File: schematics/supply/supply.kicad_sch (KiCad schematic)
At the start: 9 parts, among them J1 Conn_01x02_Pin, J2 Conn_01x01_Pin

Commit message: re-design supply board
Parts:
- added J2, J3, J5, J6: RFShield_OnePiece, Library:EMI_SHIELD_1P_2H, symbol Device:RFShield_OnePiece
- renumbered J2 to J4
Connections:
- new net GND: J2.1 (Shield), J3.1 (Shield), J5.1 (Shield), J6.1 (Shield)
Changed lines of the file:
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@@
 (kicad_sch (version 20230121) (generator eeschema)
   (paper "A3")
+  (junction (at 176.53 271.78) (diameter 0) (color 0 0 0 0)
+  )
+  (junction (at 176.53 246.38) (diameter 0) (color 0 0 0 0)
+  )
   (junction (at 88.9 96.52) (diameter 0) (color 0 0 0 0)
   )
@@
     (stroke (width 0) (type default))
   )
+  (wire (pts (xy 176.53 271.78) (xy 204.47 271.78))
+    (stroke (width 0) (type default))
+  )
   (wire (pts (xy 166.37 66.04) (xy 166.37 68.58))
     (stroke (width 0) (type default))
   )
+  (wire (pts (xy 176.53 246.38) (xy 203.2 246.38))
+    (stroke (width 0) (type default))
+  )
   (wire (pts (xy 143.51 114.3) (xy 173.99 114.3))
     (stroke (width 0) (type default))
@@
     (stroke (width 0) (type default))
   )
+  (wire (pts (xy 176.53 271.78) (xy 176.53 274.32))
+    (stroke (width 0) (type default))
+  )
   (wire (pts (xy 300.99 102.87) (xy 281.94 102.87))
     (stroke (width 0) (type default))
@@
     (stroke (width 0) (type default))
   )
+  (wire (pts (xy 149.86 270.51) (xy 149.86 271.78))
+    (stroke (width 0) (type default))
+  )
   (wire (pts (xy 71.12 62.23) (xy 88.9 62.23))
     (stroke (width 0) (type default))
@@
     (stroke (width 0) (type default))
   )
+  (wire (pts (xy 149.86 246.38) (xy 176.53 246.38))
+    (stroke (width 0) (type default))
+  )
   (wire (pts (xy 88.9 161.29) (xy 88.9 96.52))
     (stroke (width 0) (type default))
@@
     (stroke (width 0) (type default))
   )
+  (wire (pts (xy 204.47 271.78) (xy 204.47 269.24))
+    (stroke (width 0) (type default))
+  )
   (wire (pts (xy 290.83 91.44) (xy 300.99 91.44))
     (stroke (width 0) (type default))
@@
     (stroke (width 0) (type default))
   )
+  (wire (pts (xy 149.86 271.78) (xy 176.53 271.78))
+    (stroke (width 0) (type default))
+  )
   (wire (pts (xy 166.37 68.58) (xy 157.48 68.58))
     (stroke (width 0) (type default))
@@
     (stroke (width 0) (type default))
   )
+  (wire (pts (xy 149.86 243.84) (xy 149.86 246.38))
+    (stroke (width 0) (type default))
+  )
   (wire (pts (xy 168.91 107.95) (xy 143.51 107.95))
     (stroke (width 0) (type default))
@@
     (stroke (width 0) (type default))
   )
+  (wire (pts (xy 203.2 246.38) (xy 203.2 243.84))
+    (stroke (width 0) (type default))
+  )
   (wire (pts (xy 71.12 68.58) (xy 80.01 68.58))
     (stroke (width 0) (type default))
@@
   )
   (wire (pts (xy 261.62 118.11) (xy 261.62 160.02))
+    (stroke (width 0) (type default))
+  )
+  (wire (pts (xy 176.53 246.38) (xy 176.53 271.78))
     (stroke (width 0) (type default))
   )
@@
     )
   )
+  (symbol (lib_id "Device:RFShield_OnePiece") (at 149.86 233.68 0) (unit 1)
+    (in_bom yes) (on_board yes) (dnp no) (fields_autoplaced)
+    (property "Reference" "J2" (at 166.37 232.41 0)
+      (effects (font (size 1.27 1.27)) (justify left))
+    )
+    (property "Value" "RFShield_OnePiece" (at 166.37 234.95 0)
+      (effects (font (size 1.27 1.27)) (justify left))
+    )
+    (property "Footprint" "Library:EMI_SHIELD_1P_2H" (at 149.86 236.22 0)
+      (effects (font (size 1.27 1.27)) hide)
+    )
+    (property "Datasheet" "~" (at 149.86 236.22 0)
+      (effects (font (size 1.27 1.27)) hide)
+    )
+    (pin "1")
+    (instances
+      (project "supply"
+        (path "/1e139717-fcd1-4008-a6ea-4c993845e928"
+          (reference "J2") (unit 1)
+        )
+      )
+    )
+  )
   (symbol (lib_id "Mechanical:MountingHole") (at 31.75 269.24 0) (unit 1)
     (in_bom no) (on_board yes) (dnp no) (fields_autoplaced)
@@
     )
   )
+  (symbol (lib_id "Device:RFShield_OnePiece") (at 149.86 260.35 0) (unit 1)
+    (in_bom yes) (on_board yes) (dnp no) (fields_autoplaced)
+    (property "Reference" "J3" (at 166.37 259.08 0)
+      (effects (font (size 1.27 1.27)) (justify left))
+    )
+    (property "Value" "RFShield_OnePiece" (at 166.37 261.62 0)
+      (effects (font (size 1.27 1.27)) (justify left))
+    )
+    (property "Footprint" "Library:EMI_SHIELD_1P_2H" (at 149.86 262.89 0)
+      (effects (font (size 1.27 1.27)) hide)
+    )
+    (property "Datasheet" "~" (at 149.86 262.89 0)
+      (effects (font (size 1.27 1.27)) hide)
+    )
+    (pin "1")
+    (instances
+      (project "supply"
+        (path "/1e139717-fcd1-4008-a6ea-4c993845e928"
+          (reference "J3") (unit 1)
+        )
+      )
+    )
+  )
+  (symbol (lib_id "Device:RFShield_OnePiece") (at 204.47 259.08 0) (unit 1)
+    (in_bom yes) (on_board yes) (dnp no) (fields_autoplaced)
+    (property "Reference" "J6" (at 220.98 257.81 0)
+      (effects (font (size 1.27 1.27)) (justify left))
+    )
+    (property "Value" "RFShield_OnePiece" (at 220.98 260.35 0)
+      (effects (font (size 1.27 1.27)) (justify left))
+    )
+    (property "Footprint" "Library:EMI_SHIELD_1P_2H" (at 204.47 261.62 0)
+      (effects (font (size 1.27 1.27)) hide)
+    )
+    (property "Datasheet" "~" (at 204.47 261.62 0)
+      (effects (font (size 1.27 1.27)) hide)
+    )
+    (pin "1")
+    (instances
+      (project "supply"
+        (path "/1e139717-fcd1-4008-a6ea-4c993845e928"
+          (reference "J6") (unit 1)
+        )
+      )
+    )
+  )
   (symbol (lib_id "Connector:Conn_01x01_Pin") (at 157.48 52.07 270) (unit 1)
     (in_bom yes) (on_board yes) (dnp no) (fields_autoplaced)
-    (property "Reference" "J2" (at 158.75 51.435 90)
+    (property "Reference" "J4" (at 158.75 51.435 90)
       (effects (font (size 1.27 1.27)) (justify left))
     )
@@
       (project "supply"
         (path "/1e139717-fcd1-4008-a6ea-4c993845e928"
-          (reference "J2") (unit 1)
+          (reference "J4") (unit 1)
+        )
+      )
+    )
+  )
+  (symbol (lib_id "power:GND") (at 176.53 274.32 0) (unit 1)
+    (in_bom yes) (on_board yes) (dnp no) (fields_autoplaced)
+    (property "Reference" "#PWR069" (at 176.53 280.67 0)
+      (effects (font (size 1.27 1.27)) hide)
+    )
+    (property "Value" "GND" (at 176.53 279.4 0)
+      (effects (font (size 1.27 1.27)))
+    )
+    (property "Footprint" "" (at 176.53 274.32 0)
+      (effects (font (size 1.27 1.27)) hide)
+    )
+    (property "Datasheet" "" (at 176.53 274.32 0)
+      (effects (font (size 1.27 1.27)) hide)
+    )
+    (pin "1")
+    (instances
+      (project "supply"
+        (path "/1e139717-fcd1-4008-a6ea-4c993845e928/bcabd54f-a555-4409-9a4f-89c20a3d7682"
+          (reference "#PWR069") (unit 1)
+        )
+        (path "/1e139717-fcd1-4008-a6ea-4c993845e928/4671650e-ec71-47e3-a051-fc2ad6d25f63"
+          (reference "#PWR0107") (unit 1)
+        )
+        (path "/1e139717-fcd1-4008-a6ea-4c993845e928"
+          (reference "#PWR02") (unit 1)
         )
       )
@@
         )
       )
+    )
+  )
+  (symbol (lib_id "Device:RFShield_OnePiece") (at 203.2 233.68 0) (unit 1)
+    (in_bom yes) (on_board yes) (dnp no) (fields_autoplaced)
+    (property "Reference" "J5" (at 219.71 232.41 0)
+      (effects (font (size 1.27 1.27)) (justify left))
+    )
+    (property "Value" "RFShield_OnePiece" (at 219.71 234.95 0)
+      (effects (font (size 1.27 1.27)) (justify left))
+    )
+    (property "Footprint" "Library:EMI_SHIELD_1P_2H" (at 203.2 236.22 0)
+      (effects (font (size 1.27 1.27)) hide)
+    )
+    (property "Datasheet" "~" (at 203.2 236.22 0)
+      (effects (font (size 1.27 1.27)) hide)
+    )
+    (pin "1")
+    (instances
+      (project "supply"
+        (path "/1e139717-fcd1-4008-a6ea-4c993845e928"
+          (reference "J5") (unit 1)
+        )
+      )

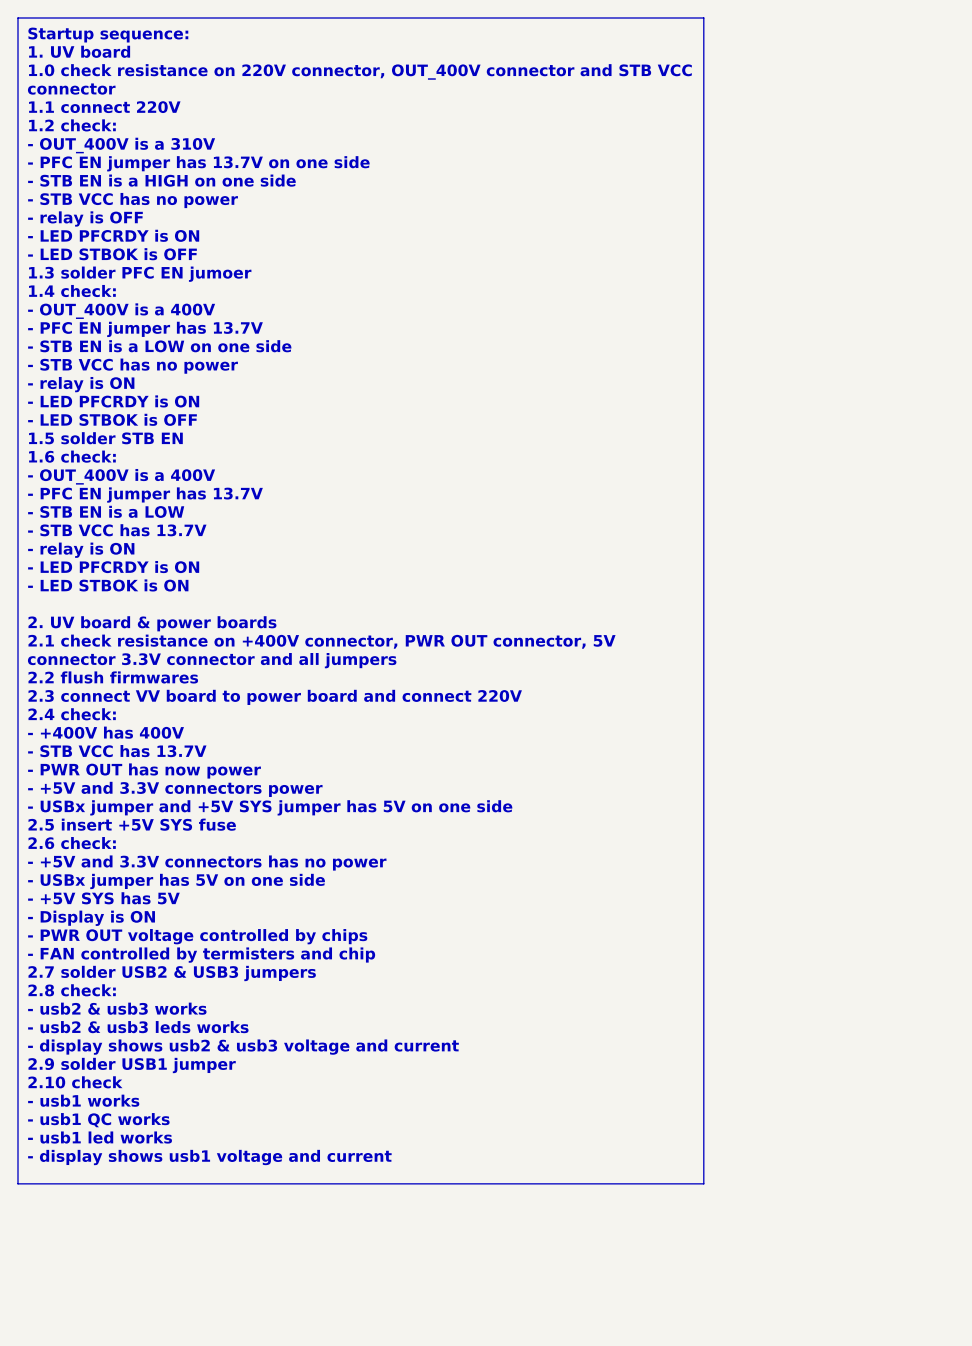
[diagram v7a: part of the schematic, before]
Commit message: debugging DCDC converters... Standby supply works fine (noise level = 1,7%). At now Starting to debug PFC module
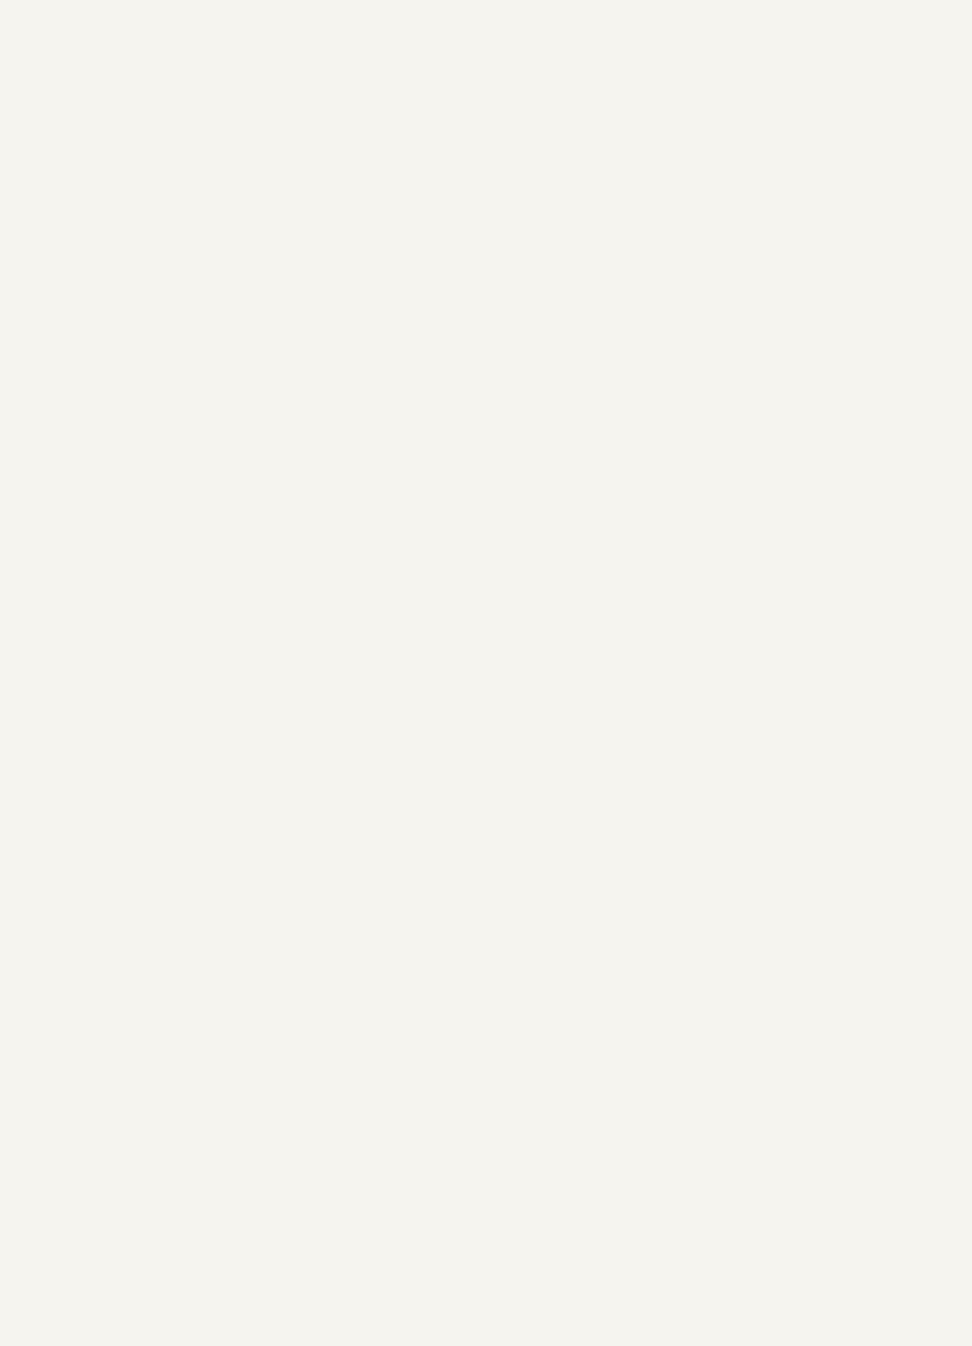
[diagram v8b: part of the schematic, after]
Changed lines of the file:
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@@
-		)
-	)
-	(text_box "Startup sequence:\n1. UV board\n1.0 check resistance on 220V connector, OUT_400V connector and STB VCC connector\n1.1 connect 220V\n1.2 check: \n    - OUT_400V is a 310V\n    - PFC EN jumper has 13.7V on one side \n    - STB EN is a HIGH on one side\n    - STB VCC has no power\n    - relay is OFF\n    - LED PFCRDY is ON\n    - LED STBOK is OFF\n1.3 solder PFC EN jumoer\n1.4 check:\n    - OUT_400V is a 400V\n    - PFC EN jumper has 13.7V\n    - STB EN is a LOW on one side\n    - STB VCC has no power\n    - relay is ON\n    - LED PFCRDY is ON\n    - LED STBOK is OFF\n1.5 solder STB EN\n1.6 check:\n    - OUT_400V is a 400V\n    - PFC EN jumper has 13.7V\n    - STB EN is a LOW\n    - STB VCC has 13.7V\n    - relay is ON\n    - LED PFCRDY is ON\n    - LED STBOK is ON\n\n2. UV board & power boards\n2.1 check resistance on +400V connector, PWR OUT connector, 5V connector 3.3V connector and all jumpers\n2.2 flush firmwares\n2.3 connect VV board to power board and connect 220V\n2.4 check:\n    - +400V has 400V\n    - STB VCC has 13.7V\n    - PWR OUT has now power\n    - +5V and 3.3V connectors power\n    - USBx jumper and +5V SYS jumper has 5V on one side\n2.5 insert +5V SYS fuse\n2.6 check:\n    - +5V and 3.3V connectors has no power\n    - USBx jumper has 5V on one side\n    - +5V SYS has 5V\n    - Display is ON\n    - PWR OUT voltage controlled by chips\n    - FAN controlled by termisters and chip\n2.7 solder USB2 & USB3 jumpers\n2.8 check: \n    - usb2 & usb3 works\n    - usb2 & usb3 leds works\n    - display shows usb2 & usb3 voltage and current\n2.9 solder USB1 jumper\n2.10 check \n    - usb1 works\n    - usb1 QC works\n    - usb1 led works\n    - display shows usb1 voltage and current\n"
-		(exclude_from_sim no)
-		(at -74.93 30.48 0)
-		(size 76.2 129.54)
-		(stroke
-			(width 0)
-			(type default)
-		)
-		(fill
-			(type none)
-		)
-		(effects
-			(font
-				(size 1.27 1.27)
-				(thickness 0.254)
-				(bold yes)
-			)
-			(justify left top)
 		)
 	)
